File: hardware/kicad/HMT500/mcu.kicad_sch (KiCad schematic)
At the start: 7 parts, among them J2 TC2030-IDC-NL, U4 STM32G0B1CCT3

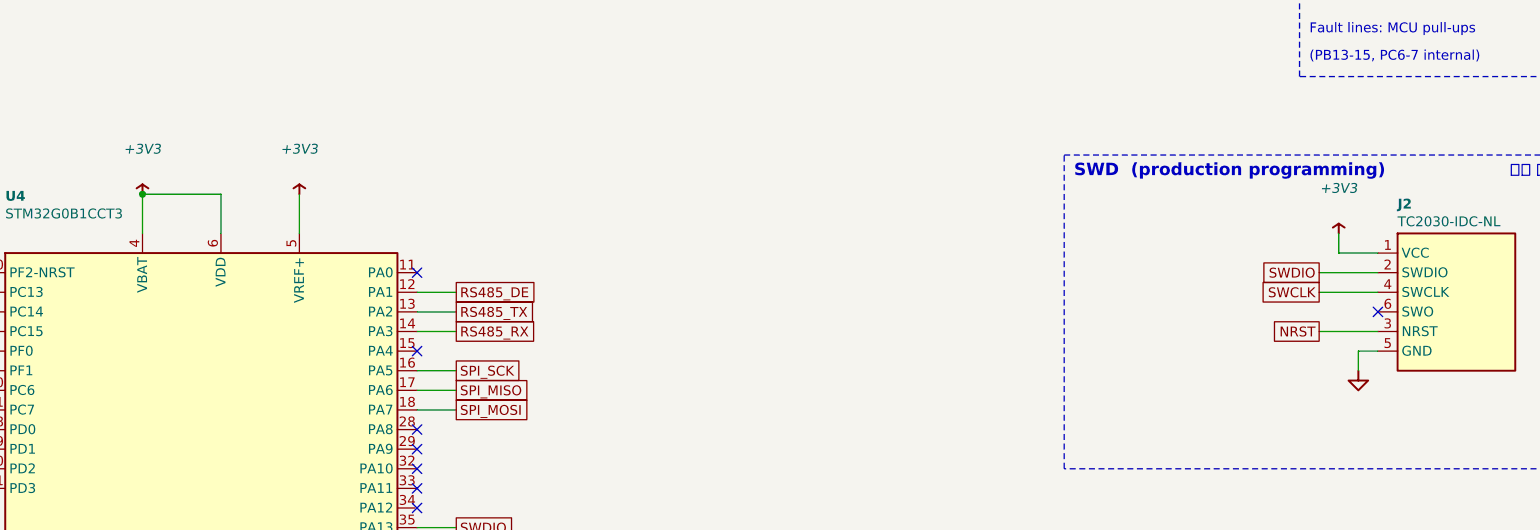
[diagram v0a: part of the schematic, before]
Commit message: Schematic redraw: aligned parts, straight wires, fewer junctions
- Bends 54 -> 1, junctions 51 -> 31 (remaining are real 3-way nodes: divider taps,
  protection taps, tied pin pairs, power flags)
- Power pins get their own power symbols instead of rails with T-branches; signals
  between distant parts use labels; two-pin parts sit on the pin row they connect to
- Symbol pin order rearranged for straight runs (pin numbers unchanged): TPS2660,
  LMR36006 (BOOT on top), PCAP04 (Cref pins 3 rows apart, VDD18 on right), ADS1220
  (bottom pins 3 apart), DAC8760 (GND-tied pins on bottom), TPS26611 (FLT on bottom)
- New checks: pin names inside IC bodies must not overlap, boxes must not overlap;
  test limits bends per sheet and total junctions
- Netlist check 63 nets, 0 errors

Co-Authored-By: Claude Opus 5.5 <noreply@anthropic.com>
Claude-Session: https://claude.ai/code/session_01JA2o8uJsqp9Vzsg4b665ev
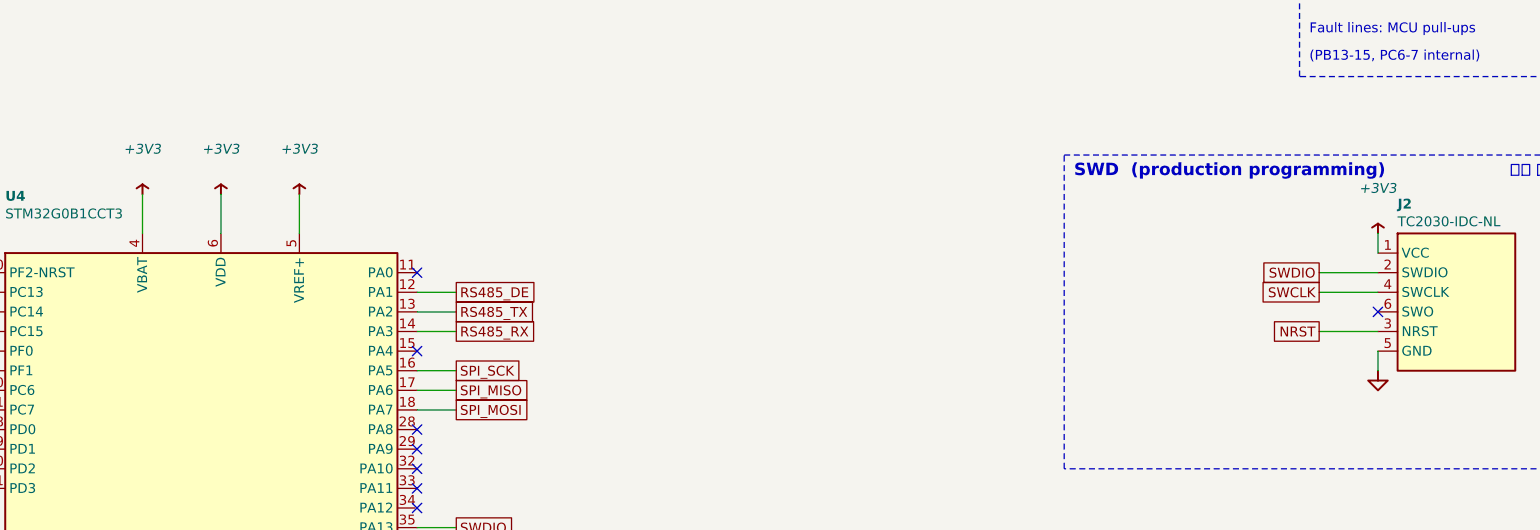
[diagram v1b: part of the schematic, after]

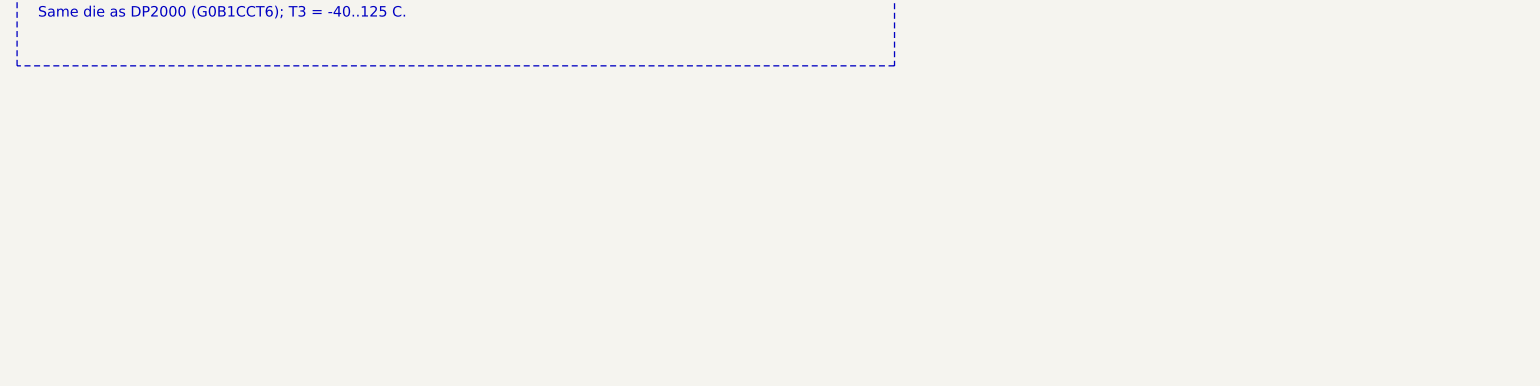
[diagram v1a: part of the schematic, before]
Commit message: Schematic: key-parts table (role, features, specs) on every sheet
- Aligned 4-column table per sheet: reference, part, role, features/specs;
  values still to confirm against datasheets marked with *
- Connector and RS-485 sheets moved to A3 for room
- New checks: text and boxes stay inside the page and out of the title block;
  every character of Hangul text must exist in NanumGothic (minus sign and micro
  sign substituted)

Co-Authored-By: Claude Opus 5.5 <noreply@anthropic.com>
Claude-Session: https://claude.ai/code/session_01JA2o8uJsqp9Vzsg4b665ev
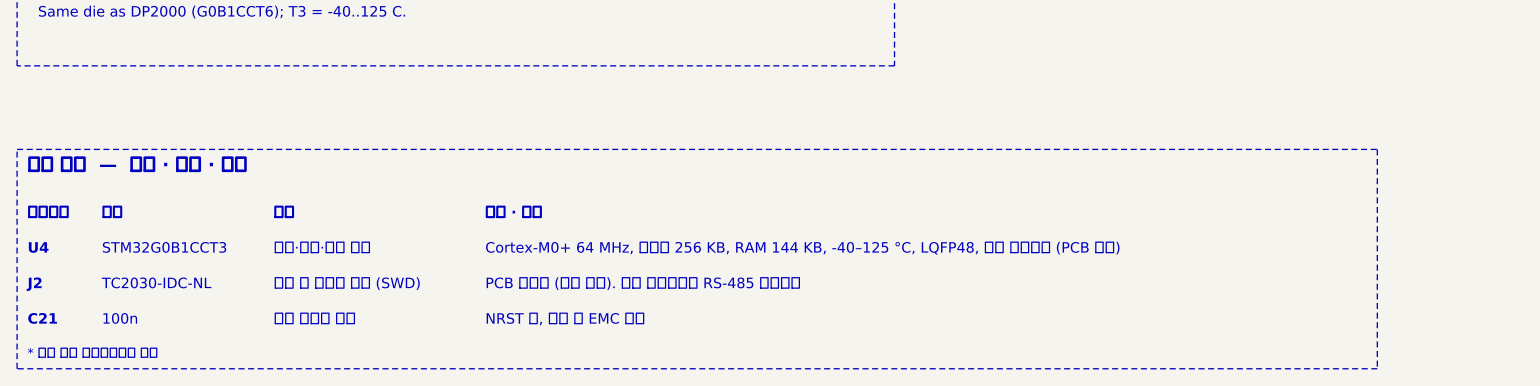
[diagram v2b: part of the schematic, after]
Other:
- note added: "* 표시 값은 데이터시트로 확인"
- note added: "100n"
- note added: "C21"
- note added: "Cortex-M0+ 64 MHz, 플래시 256 KB, RAM 144 KB, -40–125 °C, LQFP48, 내부 온도센서 (PCB 온도)"
- note added: "J2"
- note added: "NRST 핀, 몰딩 후 EMC 여유"
- note added: "PCB 패드만 (부품 없음). 이후 업데이트는 RS-485 부트로더"
- note added: "STM32G0B1CCT3"
- note added: "TC2030-IDC-NL"
- note added: "U4"
- note added: "리셋 노이즈 필터"
- note added: "부품"
- note added: "부품번호"
- note added: "생산 때 펌웨어 기록 (SWD)"
- note added: "역할"
- note added: "제어·통신·보정 연산"
- note added: "주요 부품 — 역할 · 특징 · 사양"
- note added: "특징 · 사양"
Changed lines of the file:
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@@
 (rectangle (start 284.48 93.98) (end 355.6 134.62) (stroke (width 0.1524) (type dash) (color 72 72 160 1)) (fill (type none)))
 (rectangle (start 30.48 172.72) (end 137.16 223.52) (stroke (width 0.1524) (type dash) (color 72 72 160 1)) (fill (type none)))
+(rectangle (start 30.48 233.68) (end 195.859 260.35) (stroke (width 0.1524) (type dash) (color 72 72 160 1)) (fill (type none)))
 (text "MCU DECOUPLING" (at 31.75 36.068 0) (effects (font (size 1.6 1.6) bold) (justify left bottom)))
 (text "MCU 바이패스" (at 60.9616 36.068 0) (effects (font (face "NanumGothic") (size 1.4 1.4)) (justify left bottom)))
@@
 (text "Cortex-M0+: no SWO (J2 pin 6 NC)." (at 33.02 212.09 0) (effects (font (size 1.27 1.27)) (justify left bottom)))
 (text "Same die as DP2000 (G0B1CCT6); T3 = -40..125 C." (at 33.02 217.932 0) (effects (font (size 1.27 1.27)) (justify left bottom)))
+(text "부품번호" (at 31.75 242.316 0) (effects (font (face "NanumGothic") (size 1.27 1.27) bold) (justify left bottom)))
+(text "부품" (at 40.7924 242.316 0) (effects (font (face "NanumGothic") (size 1.27 1.27) bold) (justify left bottom)))
+(text "역할" (at 61.6839 242.316 0) (effects (font (face "NanumGothic") (size 1.27 1.27) bold) (justify left bottom)))
+(text "특징 · 사양" (at 87.4014 242.316 0) (effects (font (face "NanumGothic") (size 1.27 1.27) bold) (justify left bottom)))
+(text "U4" (at 31.75 246.634 0) (effects (font (size 1.27 1.27) bold) (justify left bottom)))
+(text "STM32G0B1CCT3" (at 40.7924 246.634 0) (effects (font (size 1.27 1.27)) (justify left bottom)))
+(text "제어·통신·보정 연산" (at 61.6839 246.634 0) (effects (font (face "NanumGothic") (size 1.27 1.27)) (justify left bottom)))
+(text "Cortex-M0+ 64 MHz, 플래시 256 KB, RAM 144 KB, -40–125 °C, LQFP48, 내부 온도센서 (PCB 온도)" (at 87.4014 246.634 0) (effects (font (face "NanumGothic") (size 1.27 1.27)) (justify left bottom)))
+(text "J2" (at 31.75 250.952 0) (effects (font (size 1.27 1.27) bold) (justify left bottom)))
+(text "TC2030-IDC-NL" (at 40.7924 250.952 0) (effects (font (size 1.27 1.27)) (justify left bottom)))
+(text "생산 때 펌웨어 기록 (SWD)" (at 61.6839 250.952 0) (effects (font (face "NanumGothic") (size 1.27 1.27)) (justify left bottom)))
+(text "PCB 패드만 (부품 없음). 이후 업데이트는 RS-485 부트로더" (at 87.4014 250.952 0) (effects (font (face "NanumGothic") (size 1.27 1.27)) (justify left bottom)))
+(text "C21" (at 31.75 255.27 0) (effects (font (size 1.27 1.27) bold) (justify left bottom)))
+(text "100n" (at 40.7924 255.27 0) (effects (font (size 1.27 1.27)) (justify left bottom)))
+(text "리셋 노이즈 필터" (at 61.6839 255.27 0) (effects (font (face "NanumGothic") (size 1.27 1.27)) (justify left bottom)))
+(text "NRST 핀, 몰딩 후 EMC 여유" (at 87.4014 255.27 0) (effects (font (face "NanumGothic") (size 1.27 1.27)) (justify left bottom)))
+(text "주요 부품  —  역할 · 특징 · 사양" (at 31.75 236.728 0) (effects (font (face "NanumGothic") (size 1.6 1.6) bold) (justify left bottom)))
+(text "* 표시 값은 데이터시트로 확인" (at 31.75 259.334 0) (effects (font (face "NanumGothic") (size 1.1 1.1)) (justify left bottom)))
 )
